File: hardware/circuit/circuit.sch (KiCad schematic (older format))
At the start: 3 parts, among them SW1 SW_SPST momentary press

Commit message: Detail circuit diagram
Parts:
- added BT1: 18650 3.7V - 3500mAh, symbol Device:Battery_Cell
- added J1: Raspberry Pi Zero-W, symbol Connector:Raspberry_Pi_2_3
- added J2: USB_B_Micro, symbol Connector:USB_B_Micro
- added U1: 5V 2A buck converter, Converter_DCDC:Converter_DCDC_TRACO_TSR-1_THT, symbol Regulator_Switching:TSR_1-2415
- added U2: Battery charger module, Package_TO_SOT_SMD:SOT-23-5, symbol Battery_Management:MCP73832-2-OT
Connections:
- net labels removed: BCM15, BCM21, GND
- wire segments 5 -> 30
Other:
- note removed: "Pin 10"
- note removed: "Pin 14"
- note removed: "Pin 20"
- note removed: "Pin 40"
- moved on the sheet: D1, R1, SW1
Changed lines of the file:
@@
 EESchema Schematic File Version 4
+LIBS:circuit-cache
 EELAYER 30 0
 EELAYER END
@@
 Sheet 1 1
 Title "Epidose: Raspberry Pi contact tracing"
-Date "2020-05-20"
-Rev "1.0"
+Date "2020-06-09"
+Rev "2.0"
 Comp "Author: Diomidis Spinellis"
 Comment1 "License: CC-BY"
@@
 $EndDescr
 $Comp
-L LED:IR204A D1
-U 1 1 5EC54C71
-P 3500 1750
-F 0 "D1" H 3450 2040 50  0000 C CNN
-F 1 "Mini LED; red" H 3450 1949 50  0000 C CNN
-F 2 "LED_THT:LED_D3.0mm_IRBlack" H 3500 1925 50  0001 C CNN
-F 3 "" H 3450 1750 50  0001 C CNN
-	1    3500 1750
+L Device:Battery_Cell BT1
+U 1 1 5EDF22CD
+P 4200 4450
+F 0 "BT1" H 4318 4546 50  0000 L CNN
+F 1 "18650 3.7V - 3500mAh" H 4318 4455 50  0000 L CNN
+F 2 "" V 4200 4510 50  0001 C CNN
+F 3 "~" V 4200 4510 50  0001 C CNN
+	1    4200 4450
 	1    0    0    -1
 $EndComp
 $Comp
+L Connector:Raspberry_Pi_2_3 J1
+U 1 1 5EE0BA77
+P 7800 3800
+F 0 "J1" H 7800 5281 50  0000 C CNN
+F 1 "Raspberry Pi Zero-W" H 7800 5190 50  0000 C CNN
+F 2 "" H 7800 3800 50  0001 C CNN
+F 3 "https://www.raspberrypi.org/documentation/hardware/raspberrypi/schematics/rpi_SCH_3bplus_1p0_reduced.pdf" H 7800 3800 50  0001 C CNN
+	1    7800 3800
+	1    0    0    -1
+$EndComp
+Wire Wire Line
+	7700 5250 7700 5100
+$Comp
 L Switch:SW_SPST SW1
 U 1 1 5EC5601D
-P 3400 2250
-F 0 "SW1" H 3400 2485 50  0000 C CNN
-F 1 "SW_SPST momentary press" H 3400 2394 50  0000 C CNN
-F 2 "" H 3400 2250 50  0001 C CNN
-F 3 "~" H 3400 2250 50  0001 C CNN
-	1    3400 2250
+P 6400 3000
+F 0 "SW1" H 6400 3235 50  0000 C CNN
+F 1 "SW_SPST momentary press" H 6400 3144 50  0000 C CNN
+F 2 "" H 6400 3000 50  0001 C CNN
+F 3 "~" H 6400 3000 50  0001 C CNN
+	1    6400 3000
 	1    0    0    -1
 $EndComp
 $Comp
+L LED:IR204A D1
+U 1 1 5EC54C71
+P 6650 3800
+F 0 "D1" H 6600 4090 50  0000 C CNN
+F 1 "Mini LED; red" H 6600 3999 50  0000 C CNN
+F 2 "LED_THT:LED_D3.0mm_IRBlack" H 6650 3975 50  0001 C CNN
+F 3 "" H 6600 3800 50  0001 C CNN
+	1    6650 3800
+	1    0    0    -1
+$EndComp
+Wire Wire Line
+	7000 3800 6750 3800
+Wire Wire Line
+	6750 3800 6550 3800
+Connection ~ 6750 3800
+$Comp
 L Device:R R1
 U 1 1 5EC5713D
-P 2900 1750
-F 0 "R1" V 2693 1750 50  0000 C CNN
-F 1 "330Ω" V 2784 1750 50  0000 C CNN
-F 2 "" V 2830 1750 50  0001 C CNN
-F 3 "~" H 2900 1750 50  0001 C CNN
-	1    2900 1750
+P 6450 4200
+F 0 "R1" V 6243 4200 50  0000 C CNN
+F 1 "330Ω" V 6334 4200 50  0000 C CNN
+F 2 "" V 6380 4200 50  0001 C CNN
+F 3 "~" H 6450 4200 50  0001 C CNN
+	1    6450 4200
+	1    0    0    -1
+$EndComp
+Wire Wire Line
+	7000 3000 6600 3000
+Wire Wire Line
+	6450 3800 6450 4050
+Wire Wire Line
+	6450 4350 6450 5250
+Wire Wire Line
+	6450 5250 7700 5250
+Wire Wire Line
+	6200 3000 6100 3000
+Wire Wire Line
+	6100 5450 7600 5450
+Wire Wire Line
+	7600 5450 7600 5100
+Wire Wire Line
+	6100 3000 6100 5450
+$Comp
+L Regulator_Switching:TSR_1-2415 U1
+U 1 1 5EE1E07D
+P 5350 3950
+F 0 "U1" H 5350 4317 50  0000 C CNN
+F 1 "5V 2A buck converter" H 5350 4226 50  0000 C CNN
+F 2 "Converter_DCDC:Converter_DCDC_TRACO_TSR-1_THT" H 5350 3800 50  0001 L CIN
+F 3 "http://www.tracopower.com/products/tsr1.pdf" H 5350 3950 50  0001 C CNN
+	1    5350 3950
+	1    0    0    -1
+$EndComp
+Wire Wire Line
+	4200 4250 4200 3850
+Wire Wire Line
+	4200 3850 4950 3850
+Wire Wire Line
+	5750 3850 5850 3850
+Wire Wire Line
+	5850 3850 5850 2300
+Wire Wire Line
+	5850 2300 7600 2300
+Wire Wire Line
+	7600 2300 7600 2500
+Wire Wire Line
+	5350 4150 5350 4850
+Wire Wire Line
+	5350 5650 7800 5650
+Wire Wire Line
+	7800 5650 7800 5100
+Wire Wire Line
+	4200 4550 4200 4850
+Wire Wire Line
+	4200 4850 5350 4850
+Connection ~ 5350 4850
+Wire Wire Line
+	5350 4850 5350 5650
+$Comp
+L Battery_Management:MCP73832-2-OT U2
+U 1 1 5EE25348
+P 3200 3950
+F 0 "U2" H 3200 4431 50  0000 C CNN
+F 1 "Battery charger module" H 3200 4340 50  0000 C CNN
+F 2 "Package_TO_SOT_SMD:SOT-23-5" H 3250 3700 50  0001 L CIN
+F 3 "http://ww1.microchip.com/downloads/en/DeviceDoc/20001984g.pdf" H 3050 3900 50  0001 C CNN
+	1    3200 3950
+	1    0    0    -1
+$EndComp
+Wire Wire Line
+	3600 3850 4200 3850
+Connection ~ 4200 3850
+Wire Wire Line
+	3200 4850 4200 4850
+Wire Wire Line
+	3200 4250 3200 4850
+Connection ~ 4200 4850
+$Comp
+L Connector:USB_B_Micro J2
+U 1 1 5EE27A76
+P 3000 2850
+F 0 "J2" V 3011 3180 50  0000 L CNN
+F 1 "USB_B_Micro" V 3102 3180 50  0000 L CNN
+F 2 "" H 3150 2800 50  0001 C CNN
+F 3 "~" H 3150 2800 50  0001 C CNN
+	1    3000 2850
 	0    1    1    0
 $EndComp
 Wire Wire Line
-	3050 1750 3300 1750
-Text GLabel 4150 1750 2    50   Input ~ 0
-BCM21
+	3200 3650 3200 3150
 Wire Wire Line
-	3600 1750 4150 1750
-Text GLabel 4150 2250 2    50   Input ~ 0
-BCM15
+	2600 2850 2500 2850
 Wire Wire Line
-	3600 2250 4150 2250
-$Comp
-L power:GND #PWR1
-U 1 1 5EC58E9E
-P 2600 1750
-F 0 "#PWR1" H 2600 1500 50  0001 C CNN
-F 1 "GND" H 2605 1577 50  0000 C CNN
-F 2 "" H 2600 1750 50  0001 C CNN
-F 3 "" H 2600 1750 50  0001 C CNN
-	1    2600 1750
-	1    0    0    -1
-$EndComp
-$Comp
-L power:GND #PWR?
-U 1 1 5EC59D6F
-P 2600 2250
-F 0 "#PWR?" H 2600 2000 50  0001 C CNN
-F 1 "GND" H 2605 2077 50  0000 C CNN
-F 2 "" H 2600 2250 50  0001 C CNN
-F 3 "" H 2600 2250 50  0001 C CNN
-	1    2600 2250
-	1    0    0    -1
-$EndComp
+	2500 2850 2500 4850
 Wire Wire Line
-	2750 1750 2600 1750
-Wire Wire Line
-	3200 2250 2600 2250
-Text Notes 4200 1700 0    50   ~ 0
-Pin 40
-Text Notes 4200 2200 0    50   ~ 0
-Pin 10
-Text Notes 2500 2200 0    50   ~ 0
-Pin 14
-Text Notes 2500 1700 0    50   ~ 0
-Pin 20
+	2500 4850 3200 4850
+Connection ~ 3200 4850
 $EndSCHEMATC

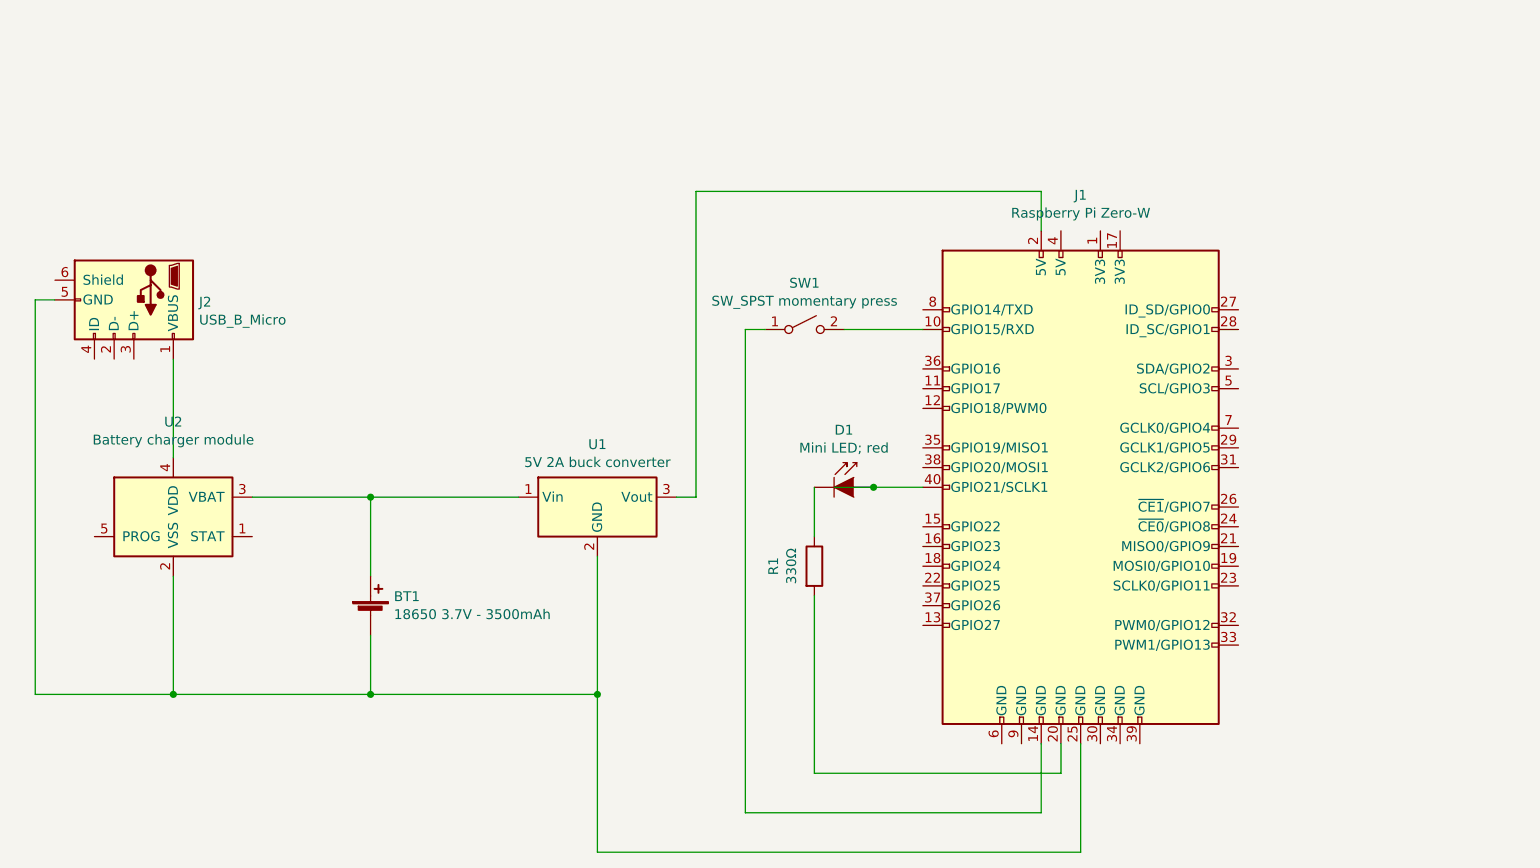
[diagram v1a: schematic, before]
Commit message: Update circuit to board-based prototype
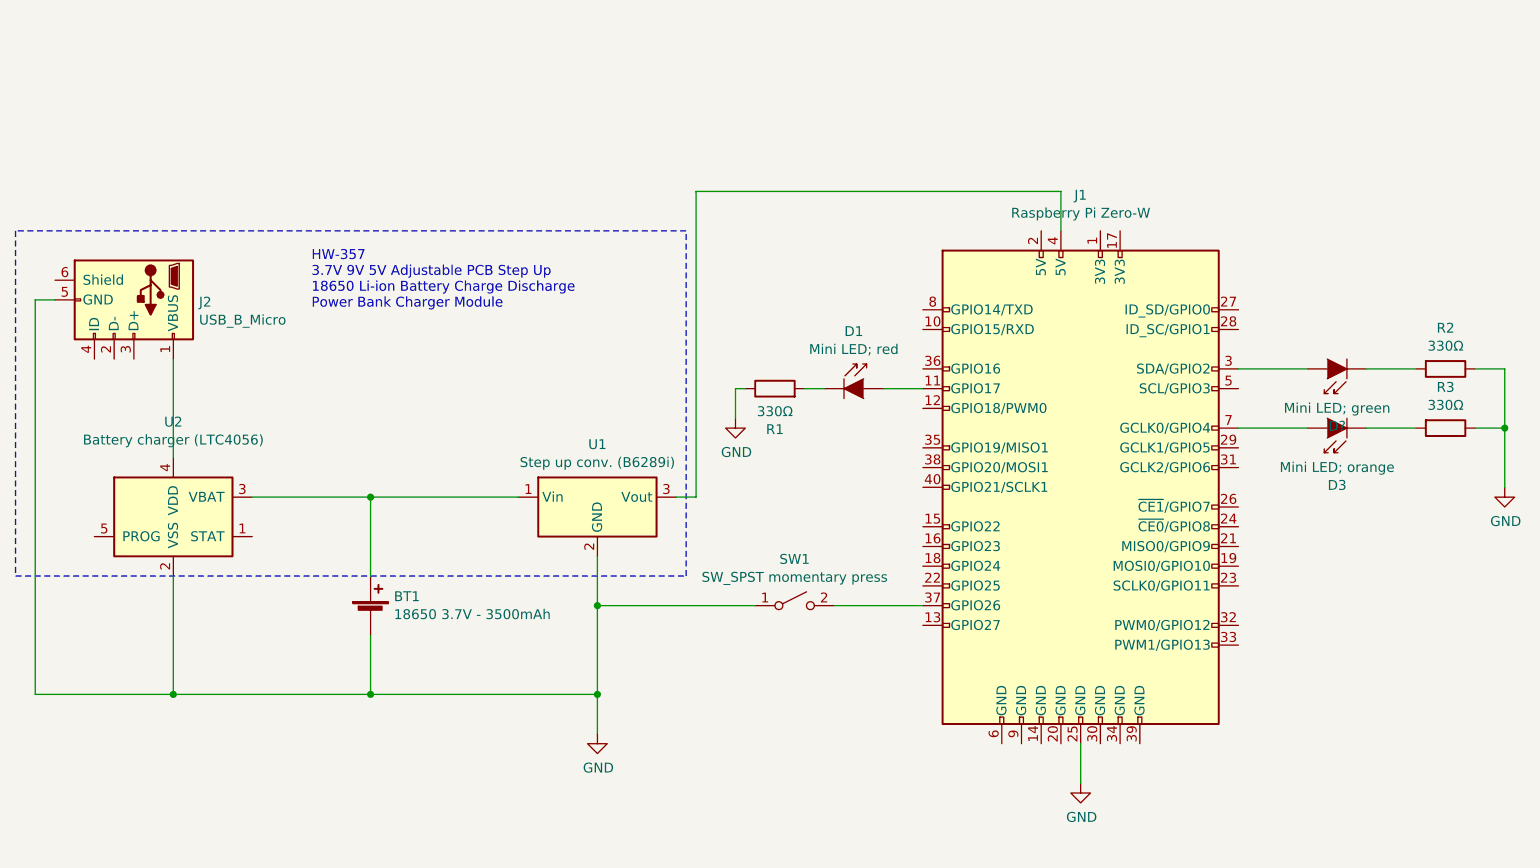
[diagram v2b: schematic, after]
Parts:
- added D3: Mini LED; orange, LED_THT:LED_D3.0mm_IRBlack, symbol LED:IR204A
- added D?: Mini LED; green, LED_THT:LED_D3.0mm_IRBlack, symbol LED:IR204A
- added R1, R2: 330Ω, symbol Device:R
- U1: value 5V 2A buck converter -> Step up conv. (B6289i)
- U2: value Battery charger module -> Battery charger (LTC4056)
- renumbered R1 to R3
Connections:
- net labels added: GND
- wire segments 30 -> 33
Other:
- note added: "HW-357\n3.7V 9V 5V Adjustable PCB Step Up \n18650 Li-ion Battery Charge Discharge\nPower Bank Charger Module"
- moved on the sheet: D1, R3, SW1
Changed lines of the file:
@@
 Sheet 1 1
 Title "Epidose: Raspberry Pi contact tracing"
-Date "2020-06-09"
-Rev "2.0"
+Date "2020-07-02"
+Rev "3.0"
 Comp "Author: Diomidis Spinellis"
 Comment1 "License: CC-BY"
@@
 	1    0    0    -1
 $EndComp
-Wire Wire Line
-	7700 5250 7700 5100
 $Comp
 L Switch:SW_SPST SW1
 U 1 1 5EC5601D
-P 6400 3000
-F 0 "SW1" H 6400 3235 50  0000 C CNN
-F 1 "SW_SPST momentary press" H 6400 3144 50  0000 C CNN
-F 2 "" H 6400 3000 50  0001 C CNN
-F 3 "~" H 6400 3000 50  0001 C CNN
-	1    6400 3000
+P 6350 4400
+F 0 "SW1" H 6350 4635 50  0000 C CNN
+F 1 "SW_SPST momentary press" H 6350 4544 50  0000 C CNN
+F 2 "" H 6350 4400 50  0001 C CNN
+F 3 "~" H 6350 4400 50  0001 C CNN
+	1    6350 4400
 	1    0    0    -1
 $EndComp
@@
 L LED:IR204A D1
 U 1 1 5EC54C71
-P 6650 3800
-F 0 "D1" H 6600 4090 50  0000 C CNN
-F 1 "Mini LED; red" H 6600 3999 50  0000 C CNN
-F 2 "LED_THT:LED_D3.0mm_IRBlack" H 6650 3975 50  0001 C CNN
-F 3 "" H 6600 3800 50  0001 C CNN
-	1    6650 3800
-	1    0    0    -1
-$EndComp
-Wire Wire Line
-	7000 3800 6750 3800
-Wire Wire Line
-	6750 3800 6550 3800
-Connection ~ 6750 3800
-$Comp
-L Device:R R1
+P 6700 3300
+F 0 "D1" H 6650 3590 50  0000 C CNN
+F 1 "Mini LED; red" H 6650 3499 50  0000 C CNN
+F 2 "LED_THT:LED_D3.0mm_IRBlack" H 6700 3475 50  0001 C CNN
+F 3 "" H 6650 3300 50  0001 C CNN
+	1    6700 3300
+	1    0    0    -1
+$EndComp
+$Comp
+L Device:R R3
 U 1 1 5EC5713D
-P 6450 4200
-F 0 "R1" V 6243 4200 50  0000 C CNN
-F 1 "330Ω" V 6334 4200 50  0000 C CNN
-F 2 "" V 6380 4200 50  0001 C CNN
-F 3 "~" H 6450 4200 50  0001 C CNN
-	1    6450 4200
-	1    0    0    -1
-$EndComp
-Wire Wire Line
-	7000 3000 6600 3000
-Wire Wire Line
-	6450 3800 6450 4050
-Wire Wire Line
-	6450 4350 6450 5250
-Wire Wire Line
-	6450 5250 7700 5250
-Wire Wire Line
-	6200 3000 6100 3000
-Wire Wire Line
-	6100 5450 7600 5450
-Wire Wire Line
-	7600 5450 7600 5100
-Wire Wire Line
-	6100 3000 6100 5450
+P 9650 3500
+F 0 "R3" V 9443 3500 50  0000 C CNN
+F 1 "330Ω" V 9534 3500 50  0000 C CNN
+F 2 "" V 9580 3500 50  0001 C CNN
+F 3 "~" H 9650 3500 50  0001 C CNN
+	1    9650 3500
+	0    1    1    0
+$EndComp
 $Comp
 L Regulator_Switching:TSR_1-2415 U1
@@
 P 5350 3950
 F 0 "U1" H 5350 4317 50  0000 C CNN
-F 1 "5V 2A buck converter" H 5350 4226 50  0000 C CNN
+F 1 "Step up conv. (B6289i)" H 5350 4226 50  0000 C CNN
 F 2 "Converter_DCDC:Converter_DCDC_TRACO_TSR-1_THT" H 5350 3800 50  0001 L CIN
 F 3 "http://www.tracopower.com/products/tsr1.pdf" H 5350 3950 50  0001 C CNN
@@
 	5850 3850 5850 2300
 Wire Wire Line
-	5850 2300 7600 2300
-Wire Wire Line
-	7600 2300 7600 2500
-Wire Wire Line
-	5350 4150 5350 4850
-Wire Wire Line
-	5350 5650 7800 5650
-Wire Wire Line
-	7800 5650 7800 5100
+	5350 4150 5350 4400
 Wire Wire Line
 	4200 4550 4200 4850
 Wire Wire Line
 	4200 4850 5350 4850
-Connection ~ 5350 4850
-Wire Wire Line
-	5350 4850 5350 5650
 $Comp
 L Battery_Management:MCP73832-2-OT U2
@@
 P 3200 3950
 F 0 "U2" H 3200 4431 50  0000 C CNN
-F 1 "Battery charger module" H 3200 4340 50  0000 C CNN
+F 1 "Battery charger (LTC4056)" H 3200 4340 50  0000 C CNN
 F 2 "Package_TO_SOT_SMD:SOT-23-5" H 3250 3700 50  0001 L CIN
 F 3 "http://ww1.microchip.com/downloads/en/DeviceDoc/20001984g.pdf" H 3050 3900 50  0001 C CNN
@@
 	2500 4850 3200 4850
 Connection ~ 3200 4850
+$Comp
+L LED:IR204A D3
+U 1 1 5EFE9B29
+P 9050 3500
+F 0 "D3" H 9000 3790 50  0000 C CNN
+F 1 "Mini LED; orange" H 9000 3699 50  0000 C CNN
+F 2 "LED_THT:LED_D3.0mm_IRBlack" H 9050 3675 50  0001 C CNN
+F 3 "" H 9000 3500 50  0001 C CNN
+	1    9050 3500
+	-1   0    0    1
+$EndComp
+$Comp
+L Device:R R2
+U 1 1 5EFE9B2F
+P 9650 3200
+F 0 "R2" V 9443 3200 50  0000 C CNN
+F 1 "330Ω" V 9534 3200 50  0000 C CNN
+F 2 "" V 9580 3200 50  0001 C CNN
+F 3 "~" H 9650 3200 50  0001 C CNN
+	1    9650 3200
+	0    1    1    0
+$EndComp
+$Comp
+L Device:R R1
+U 1 1 5EFEB41B
+P 6250 3300
+F 0 "R1" V 6043 3300 50  0000 C CNN
+F 1 "330Ω" V 6134 3300 50  0000 C CNN
+F 2 "" V 6180 3300 50  0001 C CNN
+F 3 "~" H 6250 3300 50  0001 C CNN
+	1    6250 3300
+	0    -1   -1   0
+$EndComp
+$Comp
+L LED:IR204A D?
+U 1 1 5EFEB415
+P 9050 3200
+F 0 "D?" H 9000 3490 50  0000 C CNN
+F 1 "Mini LED; green" H 9000 3399 50  0000 C CNN
+F 2 "LED_THT:LED_D3.0mm_IRBlack" H 9050 3375 50  0001 C CNN
+F 3 "" H 9000 3200 50  0001 C CNN
+	1    9050 3200
+	-1   0    0    1
+$EndComp
+Wire Wire Line
+	8600 3200 8950 3200
+$Comp
+L power:GND #PWR?
+U 1 1 5EFF21C3
+P 9950 3800
+F 0 "#PWR?" H 9950 3550 50  0001 C CNN
+F 1 "GND" H 9955 3627 50  0000 C CNN
+F 2 "" H 9950 3800 50  0001 C CNN
+F 3 "" H 9950 3800 50  0001 C CNN
+	1    9950 3800
+	1    0    0    -1
+$EndComp
+Connection ~ 5350 4400
+Wire Wire Line
+	5350 4400 5350 4850
+$Comp
+L power:GND #PWR?
+U 1 1 5EFF40C0
+P 7800 5300
+F 0 "#PWR?" H 7800 5050 50  0001 C CNN
+F 1 "GND" H 7805 5127 50  0000 C CNN
+F 2 "" H 7800 5300 50  0001 C CNN
+F 3 "" H 7800 5300 50  0001 C CNN
+	1    7800 5300
+	1    0    0    -1
+$EndComp
+Wire Wire Line
+	7700 2300 7700 2500
+Wire Wire Line
+	5850 2300 7700 2300
+Wire Wire Line
+	7800 5100 7800 5300
+Wire Wire Line
+	5350 4850 5350 5050
+Connection ~ 5350 4850
+$Comp
+L power:GND #PWR?
+U 1 1 5EFF7797
+P 5350 5050
+F 0 "#PWR?" H 5350 4800 50  0001 C CNN
+F 1 "GND" H 5355 4877 50  0000 C CNN
+F 2 "" H 5350 5050 50  0001 C CNN
+F 3 "" H 5350 5050 50  0001 C CNN
+	1    5350 5050
+	1    0    0    -1
+$EndComp
+Wire Notes Line
+	2400 2500 2400 4250
+Wire Notes Line
+	2400 4250 5800 4250
+Wire Notes Line
+	5800 4250 5800 2500
+Wire Notes Line
+	5800 2500 2400 2500
+Text Notes 3900 2900 0    50   ~ 0
+HW-357\n3.7V 9V 5V Adjustable PCB Step Up \n18650 Li-ion Battery Charge Discharge\nPower Bank Charger Module
+Wire Wire Line
+	6550 4400 7000 4400
+Wire Wire Line
+	5350 4400 6150 4400
+Wire Wire Line
+	9950 3200 9950 3500
+Wire Wire Line
+	6400 3300 6500 3300
+Wire Wire Line
+	6800 3300 7000 3300
+Wire Wire Line
+	6100 3300 6050 3300
+Wire Wire Line
+	6050 3300 6050 3450
+Wire Wire Line
+	9250 3500 9500 3500
+Wire Wire Line
+	9800 3500 9950 3500
+Wire Wire Line
+	9800 3200 9950 3200
+Wire Wire Line
+	9250 3200 9500 3200
+Wire Wire Line
+	8600 3500 8950 3500
+Wire Wire Line
+	9950 3800 9950 3500
+Connection ~ 9950 3500
+$Comp
+L power:GND #PWR?
+U 1 1 5EFF124B
+P 6050 3450
+F 0 "#PWR?" H 6050 3200 50  0001 C CNN
+F 1 "GND" H 6055 3277 50  0000 C CNN
+F 2 "" H 6050 3450 50  0001 C CNN
+F 3 "" H 6050 3450 50  0001 C CNN
+	1    6050 3450
+	1    0    0    -1
+$EndComp
 $EndSCHEMATC
